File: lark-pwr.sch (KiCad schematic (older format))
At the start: 47 parts

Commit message: Finalize schematic
Finish part selection

Pending issues: IMU, switches & LEDs, mechanical parts and housing
selection.
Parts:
- removed D?: Transil, symbol Device:D_Schottky
- added D4: 16V, Diode_SMD:D_SMB_Handsoldering, symbol Device:D_Zener
- C10: renamed from C?; footprint (none) -> Capacitor_SMD:CP_Elec_16x17.5; MPN (none) -> UUE1H331MNS1MS
- C11, C17, C30, C32, C8: renamed from C?; footprint (none) -> Capacitor_SMD:C_0805_2012Metric_Pad1.15x1.40mm_HandSolder; MPN (none) -> 885012207128
- C12, C21, C22, C23, C24, C25, C26, C27, C28, C29, C9: renamed from C?; footprint (none) -> Capacitor_SMD:C_0805_2012Metric_Pad1.15x1.40mm_HandSolder; MPN (none) -> CL21B105KBFNNNG
- C13, C14: renamed from 22u; value C -> 100n; footprint (none) -> Capacitor_SMD:C_0805_2012Metric_Pad1.15x1.40mm_HandSolder; MPN (none) -> 885012207128
- C15: renamed from 100n; value C -> 22u; footprint (none) -> Capacitor_SMD:C_0805_2012Metric_Pad1.15x1.40mm_HandSolder; MPN (none) -> GRM21BD70J226ME44L
- C16: renamed from C?; footprint (none) -> Capacitor_SMD:CP_Elec_16x17.5; MPN (none) -> 493-16063-1-ND
- C18, C19, C20: renamed from C?; footprint (none) -> Capacitor_SMD:C_0805_2012Metric_Pad1.15x1.40mm_HandSolder
- C31: renamed from C?; value 100n -> 1u; footprint (none) -> Capacitor_SMD:C_0805_2012Metric_Pad1.15x1.40mm_HandSolder; MPN (none) -> CL21B105KBFNNNG
- D3, D5: renamed from D?; value SK35 -> 50V/3A; footprint (none) -> Diode_SMD:D_SMC_Handsoldering; MPN (none) -> SK35
- J4: renamed from J?; value Screw_Terminal_01x02 -> PWR_IN; footprint (none) -> TerminalBlock_Phoenix:TerminalBlock_Phoenix_PT-1,5-2-3.5-H_1x02_P3.50mm_Horizontal; MPN (none) -> 277-1721-ND
- L1: renamed from L?; value Ferrite_Bead -> 6A max.; footprint (none) -> Inductor_SMD:L_1206_3216Metric_Pad1.42x1.75mm_HandSolder; MPN (none) -> BLM31KN121SN1L
- L2, L4, L5, L7: renamed from L?; footprint (none) -> Inductor_SMD:L_0805_2012Metric_Pad1.15x1.40mm_HandSolder; MPN (none) -> BLM21BD272SH1L
- L3: renamed from L?; value 33uH, L40 -> 47uH/3.5A; footprint (none) -> Inductor_SMD:L_12x12mm_H8mm; MPN (none) -> SRR1210A-470MCT-ND
- L6: renamed from L?; footprint (none) -> Inductor_SMD:L_1206_3216Metric_Pad1.42x1.75mm_HandSolder; MPN (none) -> BLM31KN121SN1L
- R25: renamed from R?; footprint (none) -> Resistor_SMD:R_0805_2012Metric_Pad1.15x1.40mm_HandSolder; MPN (none) -> RC0805FR-0710KL
- R26: renamed from R?; footprint (none) -> Resistor_SMD:R_0805_2012Metric_Pad1.15x1.40mm_HandSolder; MPN (none) -> RC0805FR-0722KL
- RV1: renamed from RV?; value Varistor -> 3A/24V; footprint (none) -> Fuse:Fuse_2920_7451Metric_Pad2.10x5.45mm_HandSolder; MPN (none) -> 0ZCF0300BF2C
- U7: renamed from U?; footprint (none) -> Package_SO:MSOP-8-1EP_3x3mm_P0.65mm_EP1.68x1.88mm; MPN (none) -> TPS2511DGNR
- gave numbers to parts that had none: 7
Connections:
- wire segments 147 -> 151

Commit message: Fill in all remaining PNs in the schematics
Finish the part selection, let's hope for least possible number of mistakes.
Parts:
- C18, C19, C20: MPN (none) -> CL21B105KBFNNNG
- U1: MPN (none) -> AZ1117EH-3.3TRG1
- U2: MPN (none) -> LM2596SX-5.0/NOPBCT-ND
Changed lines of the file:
@@
 F 2 "Package_TO_SOT_SMD:SOT-223-3_TabPin2" H 8800 1550 50  0001 C CNN
 F 3 "http://www.diodes.com/datasheets/AP1117.pdf" H 8900 1100 50  0001 C CNN
+F 4 "AZ1117EH-3.3TRG1" H 8800 1350 50  0001 C CNN "MPN"
 	1    8800 1350
 	1    0    0    -1
@@
 F 2 "Capacitor_SMD:C_0805_2012Metric_Pad1.15x1.40mm_HandSolder" H 6488 2750 50  0001 C CNN
 F 3 "~" H 6450 2900 50  0001 C CNN
+F 4 "CL21B105KBFNNNG" H 0   0   50  0001 C CNN "MPN"
 	1    6450 2900
 	1    0    0    -1
@@
 F 2 "Capacitor_SMD:C_0805_2012Metric_Pad1.15x1.40mm_HandSolder" H 8138 2750 50  0001 C CNN
 F 3 "~" H 8100 2900 50  0001 C CNN
+F 4 "CL21B105KBFNNNG" H 0   0   50  0001 C CNN "MPN"
 	1    8100 2900
 	1    0    0    -1
@@
 F 2 "Capacitor_SMD:C_0805_2012Metric_Pad1.15x1.40mm_HandSolder" H 9538 2750 50  0001 C CNN
 F 3 "~" H 9500 2900 50  0001 C CNN
+F 4 "CL21B105KBFNNNG" H 0   0   50  0001 C CNN "MPN"
 	1    9500 2900
 	1    0    0    -1
@@
 F 2 "Package_TO_SOT_SMD:TO-263-5_TabPin3" H 2750 2350 50  0001 L CIN
 F 3 "http://www.ti.com/lit/ds/symlink/lm2596.pdf" H 2700 2600 50  0001 C CNN
+F 4 "LM2596SX-5.0/NOPBCT-ND" H 0   0   50  0001 C CNN "MPN"
 	1    2700 2600
 	1    0    0    -1
@@
 U 1 1 5C5A2D6B
 P 3100 5700
+AR Path="/5C5A2D6B" Ref="U7"  Part="1"
+AR Path="/5C42B39D/5C5A2D6B" Ref="U7"  Part="1"
 F 0 "U7" H 3100 6265 50  0000 C CNN
 F 1 "TPS2511" H 3100 6174 50  0000 C CNN

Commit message: Intermediate status while arranging compontents.
Manually grouped components into smaller islands.

Some parts were changed:
* U1: SOT-23-3 LDO should be sufficient
* CP_Elec: Use 10x10 size
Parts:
- removed U1: AP1117-33, Package_TO_SOT_SMD:SOT-223-3_TabPin2, symbol Regulator_Linear:AP1117-33
- added U1: MCP1700T-3302E_TT, Package_TO_SOT_SMD:SOT-23, symbol lark-rescue:MCP1700T-3302E_TT-dk_PMIC-Voltage-Regulators-Linear
- C10, C16: footprint Capacitor_SMD:CP_Elec_16x17.5 -> Capacitor_SMD:CP_Elec_10x10
- D3, D5: footprint Diode_SMD:D_SMC_Handsoldering -> Diode_SMD:D_SOD-123
- D4: footprint Diode_SMD:D_SMB_Handsoldering -> Diode_SMD:D_SOD-123
- J5: symbol dk_USB-DVI-HDMI-Connectors:UE27AC54100 -> lark-rescue:UE27AC54100-dk_USB-DVI-HDMI-Connectors
- U3, U4, U5, U6: footprint digikey-footprints:SOT-23-3 -> Package_TO_SOT_SMD:SOT-23; symbol dk_PMIC-Voltage-Regulators-Linear:MCP1700T-3302E_TT -> lark-rescue:MCP1700T-3302E_TT-dk_PMIC-Voltage-Regulators-Linear
- U7: symbol tps2511:TPS2511 -> lark-rescue:TPS2511-tps2511

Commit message: continue layout work, WIP
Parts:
- C10, C16: symbol Device:CP -> lark-rescue:CP-Device
- C11, C12, C13, C14, C15, C17, C18, C19, C20, C21, C22, C23, C24, C25, C26, C27, C28, C29, C30, C31, C32, C8, C9: symbol Device:C -> lark-rescue:C-Device
- D3, D5: symbol Device:D_Schottky -> lark-rescue:D_Schottky-Device
- D4: symbol Device:D_Zener -> lark-rescue:D_Zener-Device
- J4: symbol Connector:Screw_Terminal_01x02 -> lark-rescue:Screw_Terminal_01x02-Connector
- L1, L2, L4, L5, L6, L7: symbol Device:Ferrite_Bead -> lark-rescue:Ferrite_Bead-Device
- L3: symbol pspice:INDUCTOR -> lark-rescue:INDUCTOR-pspice
- R25, R26: symbol Device:R -> lark-rescue:R-Device
- RV1: symbol Device:Varistor -> lark-rescue:Varistor-Device
- U2: symbol Regulator_Switching:LM2596S-5 -> lark-rescue:LM2596S-5-Regulator_Switching
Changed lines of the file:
@@
 $EndDescr
 $Comp
-L power:+5V #PWR?
+L lark-rescue:+5V-power #PWR?
 U 1 1 5C42BB67
 P 7850 1350
@@
 $EndComp
 $Comp
-L Device:C C?
+L lark-rescue:C-Device C?
 U 1 1 5C42BB6D
 P 8150 1500
@@
 	9100 1350 9500 1350
 $Comp
-L Device:C C?
+L lark-rescue:C-Device C?
 U 1 1 5C42BB7B
 P 9500 1500
@@
 	9500 1350 9950 1350
 $Comp
-L Device:C C?
+L lark-rescue:C-Device C?
 U 1 1 5C42BB84
 P 9950 1500
@@
 	9500 1650 8800 1650
 $Comp
-L power:VDD #PWR?
+L lark-rescue:VDD-power #PWR?
 U 1 1 5C42BB90
 P 10300 1350
@@
 $EndComp
 $Comp
-L power:GND #PWR?
+L lark-rescue:GND-power #PWR?
 U 1 1 5C42BC85
 P 8800 1850
@@
 $EndComp
 $Comp
-L power:GND #PWR019
+L lark-rescue:GND-power #PWR019
 U 1 1 5C53A890
 P 1350 1300
@@
 $EndComp
 $Comp
-L Device:Varistor RV1
+L lark-rescue:Varistor-Device RV1
 U 1 1 5C5396E1
 P 1750 1000
@@
 $EndComp
 $Comp
-L Device:C C8
+L lark-rescue:C-Device C8
 U 1 1 5C539CEA
 P 3200 1150
@@
 $EndComp
 $Comp
-L Device:C C9
+L lark-rescue:C-Device C9
 U 1 1 5C539D44
 P 3800 1150
@@
 $EndComp
 $Comp
-L Device:Ferrite_Bead L1
+L lark-rescue:Ferrite_Bead-Device L1
 U 1 1 5C53A44D
 P 4500 1000
@@
 $EndComp
 $Comp
-L Device:CP C10
+L lark-rescue:CP-Device C10
 U 1 1 5C53A4E4
 P 5050 1150
@@
 $EndComp
 $Comp
-L Device:C C11
+L lark-rescue:C-Device C11
 U 1 1 5C53A54F
 P 5650 1150
@@
 $EndComp
 $Comp
-L Device:C C12
+L lark-rescue:C-Device C12
 U 1 1 5C53A5CA
 P 6200 1150
@@
 Connection ~ 1350 1300
 $Comp
-L power:+12V #PWR016
+L lark-rescue:+12V-power #PWR016
 U 1 1 5C53DB37
 P 6600 1000
@@
 	6600 1000 6800 1000
 $Comp
-L power:+5V #PWR021
+L lark-rescue:+5V-power #PWR021
 U 1 1 5C53E61A
 P 4950 1950
@@
 $EndComp
 $Comp
-L power:+12V #PWR022
+L lark-rescue:+12V-power #PWR022
 U 1 1 5C53E670
 P 1100 2000
@@
 $EndComp
 $Comp
-L power:GND #PWR024
+L lark-rescue:GND-power #PWR024
 U 1 1 5C53E79D
 P 2750 2750
@@
 $EndComp
 $Comp
-L pspice:INDUCTOR L3
+L lark-rescue:INDUCTOR-pspice L3
 U 1 1 5C53E9E4
 P 3850 2300
@@
 $EndComp
 $Comp
-L Device:CP C16
+L lark-rescue:CP-Device C16
 U 1 1 5C53EA82
 P 4400 2450
@@
 $EndComp
 $Comp
-L Device:C C17
+L lark-rescue:C-Device C17
 U 1 1 5C53EB34
 P 4950 2450
@@
 $EndComp
 $Comp
-L Device:D_Schottky D5
+L lark-rescue:D_Schottky-Device D5
 U 1 1 5C53F38F
 P 3400 2450
@@
 $EndComp
 $Comp
-L Device:C C21
+L lark-rescue:C-Device C21
 U 1 1 5C54D321
 P 900 3850
@@
 $EndComp
 $Comp
-L power:+5V #PWR026
+L lark-rescue:+5V-power #PWR026
 U 1 1 5C54D45D
 P 900 3350
@@
 PSTATPWR
 $Comp
-L power:GND #PWR028
+L lark-rescue:GND-power #PWR028
 U 1 1 5C54D567
 P 2050 4100
@@
 $EndComp
 $Comp
-L Device:C C22
+L lark-rescue:C-Device C22
 U 1 1 5C54D5CF
 P 2550 3850
@@
 $EndComp
 $Comp
-L Device:C C23
+L lark-rescue:C-Device C23
 U 1 1 5C54D68B
 P 3950 3850
@@
 $EndComp
 $Comp
-L Device:Ferrite_Bead L4
+L lark-rescue:Ferrite_Bead-Device L4
 U 1 1 5C54D8CC
 P 3250 3600
@@
 $EndComp
 $Comp
-L Device:C C27
+L lark-rescue:C-Device C27
 U 1 1 5C56106D
 P 900 5200
@@
 $EndComp
 $Comp
-L power:+5V #PWR031
+L lark-rescue:+5V-power #PWR031
 U 1 1 5C561073
 P 900 4700
@@
 PDIFPWR
 $Comp
-L power:GND #PWR033
+L lark-rescue:GND-power #PWR033
 U 1 1 5C56107A
 P 2050 5450
@@
 $EndComp
 $Comp
-L Device:C C28
+L lark-rescue:C-Device C28
 U 1 1 5C561080
 P 2550 5200
@@
 $EndComp
 $Comp
-L Device:C C29
+L lark-rescue:C-Device C29
 U 1 1 5C561086
 P 3950 5200
@@
 $EndComp
 $Comp
-L Device:Ferrite_Bead L7
+L lark-rescue:Ferrite_Bead-Device L7
 U 1 1 5C56108C
 P 3250 4950
@@
 $EndComp
 $Comp
-L Device:C C24
+L lark-rescue:C-Device C24
 U 1 1 5C5634DD
 P 5100 5200
@@
 $EndComp
 $Comp
-L power:+5V #PWR027
+L lark-rescue:+5V-power #PWR027
 U 1 1 5C5634E3
 P 5100 4700
@@
 PDUSPWR
 $Comp
-L power:GND #PWR029
+L lark-rescue:GND-power #PWR029
 U 1 1 5C5634EA
 P 6250 5450
@@
 $EndComp
 $Comp
-L Device:C C25
+L lark-rescue:C-Device C25
 U 1 1 5C5634F0
 P 6750 5200
@@
 $EndComp
 $Comp
-L Device:C C26
+L lark-rescue:C-Device C26
 U 1 1 5C5634F6
 P 8150 5200
@@
 $EndComp
 $Comp
-L Device:Ferrite_Bead L5
+L lark-rescue:Ferrite_Bead-Device L5
 U 1 1 5C5634FC
 P 7450 4950
@@
 $EndComp
 $Comp
-L Device:C C18
+L lark-rescue:C-Device C18
 U 1 1 5C56951F
 P 5100 3850
@@
 $EndComp
 $Comp
-L power:+5V #PWR023
+L lark-rescue:+5V-power #PWR023
 U 1 1 5C569525
 P 5100 3350
@@
 ACCELPWR
 $Comp
-L power:GND #PWR025
+L lark-rescue:GND-power #PWR025
 U 1 1 5C56952C
 P 6250 4100
@@
 $EndComp
 $Comp
-L Device:C C19
+L lark-rescue:C-Device C19
 U 1 1 5C569532
 P 6750 3850
@@
 $EndComp
 $Comp
-L Device:C C20
+L lark-rescue:C-Device C20
 U 1 1 5C569538
 P 8150 3850
@@
 $EndComp
 $Comp
-L Device:Ferrite_Bead L2
+L lark-rescue:Ferrite_Bead-Device L2
 U 1 1 5C56953E
 P 7450 3600
@@
 Connection ~ 5100 3600
 $Comp
-L Regulator_Switching:LM2596S-5 U2
+L lark-rescue:LM2596S-5-Regulator_Switching U2
 U 1 1 5C5806FE
 P 2750 2200
@@
 $EndComp
 $Comp
-L Device:D_Schottky D3
+L lark-rescue:D_Schottky-Device D3
 U 1 1 5C5A21AF
 P 2750 1000
@@
 $EndComp
 $Comp
-L power:GND #PWR034
+L lark-rescue:GND-power #PWR034
 U 1 1 5C5B50B6
 P 650 7550
@@
 $EndComp
 $Comp
-L power:+5V #PWR032
+L lark-rescue:+5V-power #PWR032
 U 1 1 5C5B51A7
 P 650 6850
@@
 	650  7500 650  7550
 $Comp
-L Device:C C30
+L lark-rescue:C-Device C30
 U 1 1 5C5C48EA
 P 650 7100
@@
 NoConn ~ 1500 7050
 $Comp
-L Device:C C31
+L lark-rescue:C-Device C31
 U 1 1 5C5E174B
 P 3200 7200
@@
 Connection ~ 650  7500
 $Comp
-L Device:R R26
+L lark-rescue:R-Device R26
 U 1 1 5C60C329
 P 1200 7150
@@
 	1200 6650 1500 6650
 $Comp
-L Device:R R25
+L lark-rescue:R-Device R25
 U 1 1 5C62DF3A
 P 850 6150
@@
 	850  6850 650  6850
 $Comp
-L Device:Ferrite_Bead L6
+L lark-rescue:Ferrite_Bead-Device L6
 U 1 1 5C63A448
 P 3500 6450
@@
 $EndComp
 $Comp
-L Device:C C32
+L lark-rescue:C-Device C32
 U 1 1 5C63A750
 P 3750 7200
@@
 	3000 6650 3950 6650
 $Comp
-L Connector:Screw_Terminal_01x02 J4
+L lark-rescue:Screw_Terminal_01x02-Connector J4
 U 1 1 5C676D1E
 P 800 1000
@@
 $EndComp
 $Comp
-L power:GND #PWR030
+L lark-rescue:GND-power #PWR030
 U 1 1 5C754FF4
 P 4650 6050
@@
 	3000 7050 3100 7050
 $Comp
-L power:PWR_FLAG #FLG01
+L lark-rescue:PWR_FLAG-power #FLG01
 U 1 1 5C7856F5
 P 1250 1000
@@
 	4400 2300 4950 2300
 $Comp
-L Device:D_Zener D4
+L lark-rescue:D_Zener-Device D4
 U 1 1 5C78CD79
 P 2200 1150

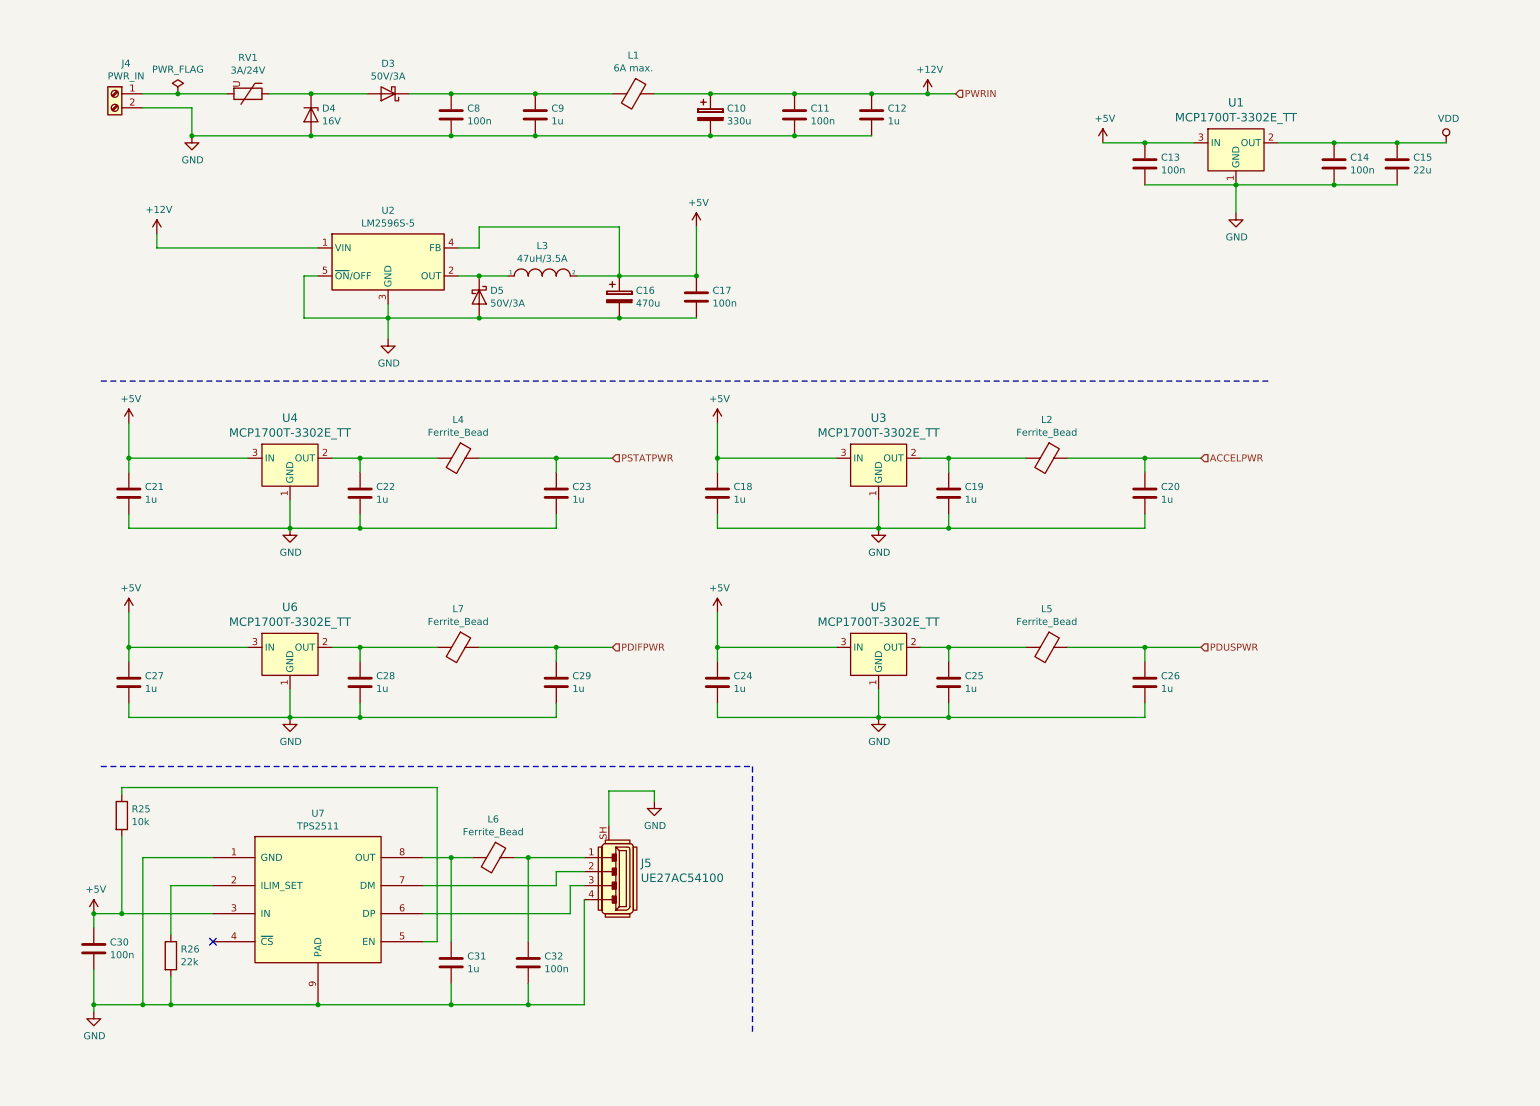
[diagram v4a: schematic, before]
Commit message: Updating schematic for the first prototype
* U1 can supply up to 600 mA
* drop USB charger for now
* smaller type of DC/DC (U2) for input
* remove one of the large capacitors
* change BMX interface to 4-wire SPI for speed reasons
* add I2C mux for pressure sensors

The changes were made during the meeting with Tomas.

BMX055 will be replaced by BMX088. For mechanical reasons, the pressure
sensors will be placed on a daughterboard. The daughterboard could get
footprints for different kinds pressure sensors (i.e. BMP388, HCLA0025).
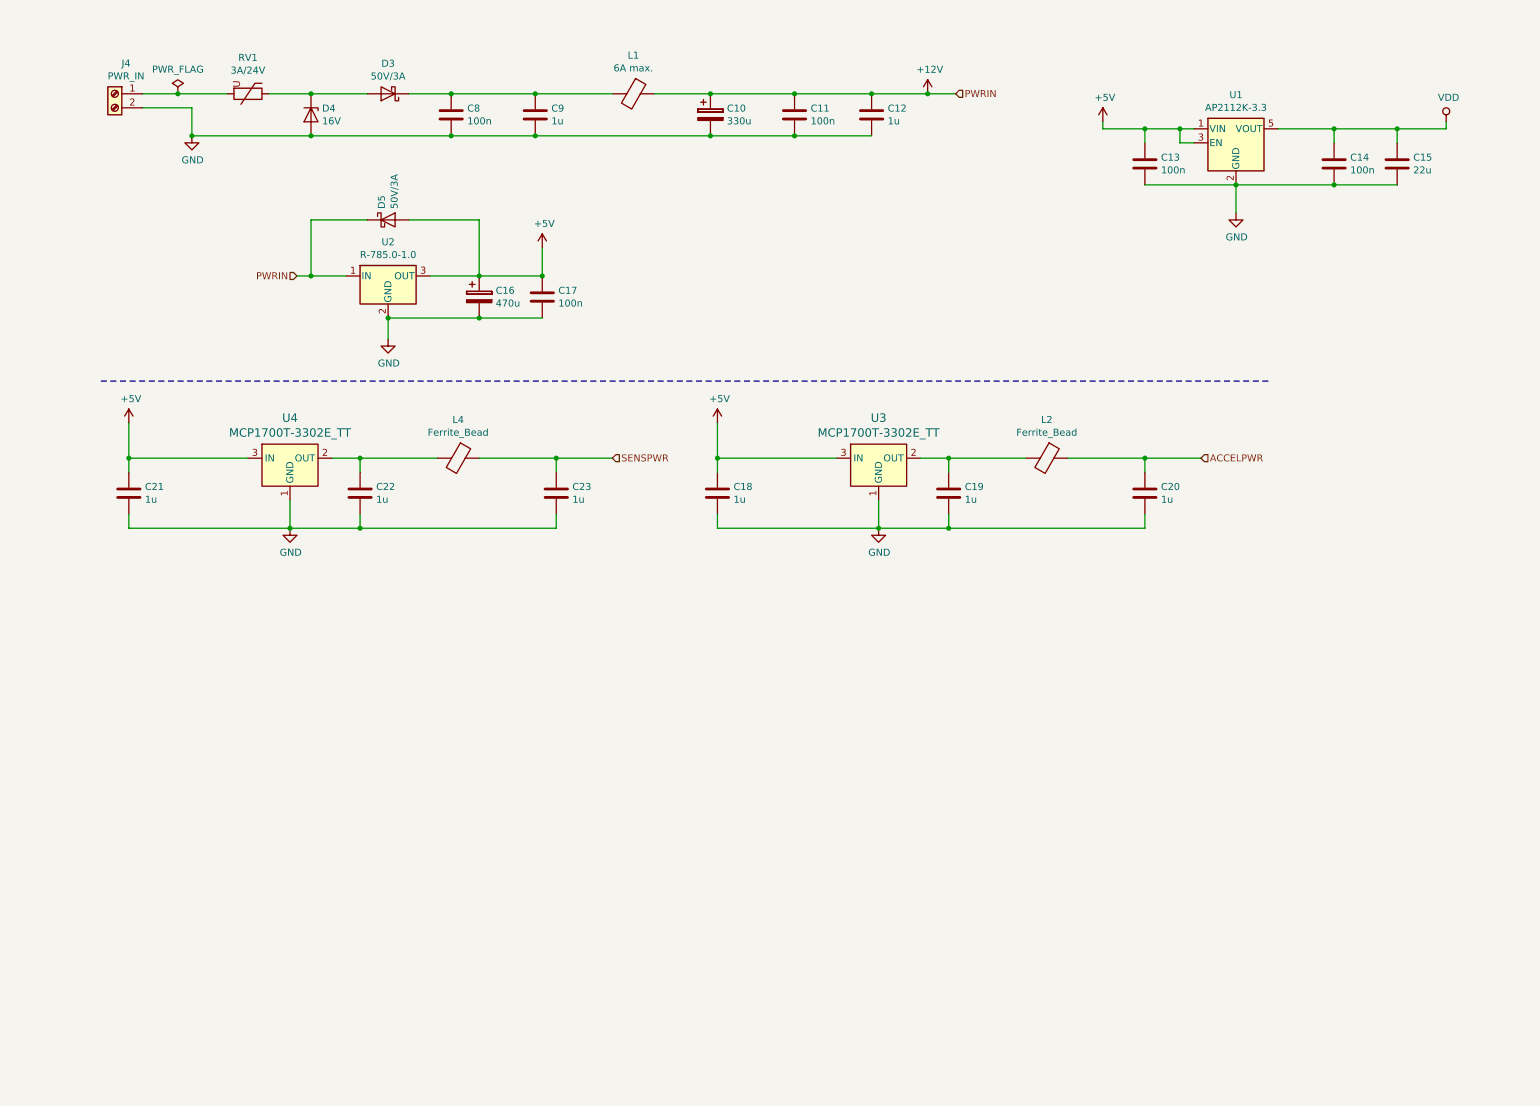
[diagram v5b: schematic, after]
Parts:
- removed C24, C25, C26, C27, C28, C29, C31: 1u, Capacitor_SMD:C_0805_2012Metric_Pad1.15x1.40mm_HandSolder, symbol lark-rescue:C-Device
- removed C30, C32: 100n, Capacitor_SMD:C_0805_2012Metric_Pad1.15x1.40mm_HandSolder, symbol lark-rescue:C-Device
- removed J5: UE27AC54100, digikey-footprints:USB_A_Female_UE27AC54100, symbol lark-rescue:UE27AC54100-dk_USB-DVI-HDMI-Connectors
- removed L3: 47uH/3.5A, Inductor_SMD:L_12x12mm_H8mm, symbol lark-rescue:INDUCTOR-pspice
- removed L5, L7: Ferrite_Bead, Inductor_SMD:L_0805_2012Metric_Pad1.15x1.40mm_HandSolder, symbol lark-rescue:Ferrite_Bead-Device
- removed L6: Ferrite_Bead, Inductor_SMD:L_1206_3216Metric_Pad1.42x1.75mm_HandSolder, symbol lark-rescue:Ferrite_Bead-Device
- removed R25: 10k, Resistor_SMD:R_0805_2012Metric_Pad1.15x1.40mm_HandSolder, symbol lark-rescue:R-Device
- removed R26: 22k, Resistor_SMD:R_0805_2012Metric_Pad1.15x1.40mm_HandSolder, symbol lark-rescue:R-Device
- removed U1, U5, U6: MCP1700T-3302E_TT, Package_TO_SOT_SMD:SOT-23, symbol lark-rescue:MCP1700T-3302E_TT-dk_PMIC-Voltage-Regulators-Linear
- removed U2: LM2596S-5, Package_TO_SOT_SMD:TO-263-5_TabPin3, symbol lark-rescue:LM2596S-5-Regulator_Switching
- removed U7: TPS2511, Package_SO:MSOP-8-1EP_3x3mm_P0.65mm_EP1.68x1.88mm, symbol lark-rescue:TPS2511-tps2511
- added U1: AP2112K-3.3, Package_TO_SOT_SMD:SOT-23-5, symbol Regulator_Linear:AP2112K-3.3
- added U2: R-785.0-1.0, Converter_DCDC:Converter_DCDC_RECOM_R-78E-0.5_THT, symbol Regulator_Switching:R-785.0-1.0
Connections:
- net +12V: now also D5.1 (K), U2.1 (IN)
- net +5V: now also D5.2 (A), U1.1 (VIN), U1.3 (EN), U2.3 (OUT)
- net GND: now also U1.2 (GND), U2.2 (GND); no longer D5.2 (A)
- net VDD: now also U1.5 (VOUT)
- net PSTATPWR renamed SENSPWR
- no-connect marks 1 -> 0
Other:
- moved on the sheet: C16, C17, D5
